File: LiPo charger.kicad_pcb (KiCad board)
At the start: 2 copper layers, 30 x 11 mm, 8 parts, among them J1 Conn_01x02, P1 USB_C_Plug_USB2.0, U1 MCP73831-2-OT

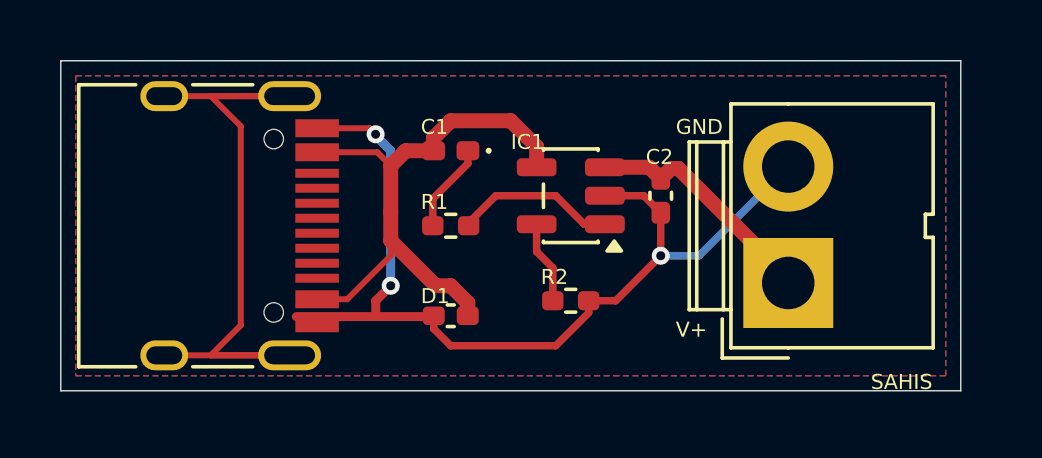
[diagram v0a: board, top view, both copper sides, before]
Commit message: PCB Trace Edited
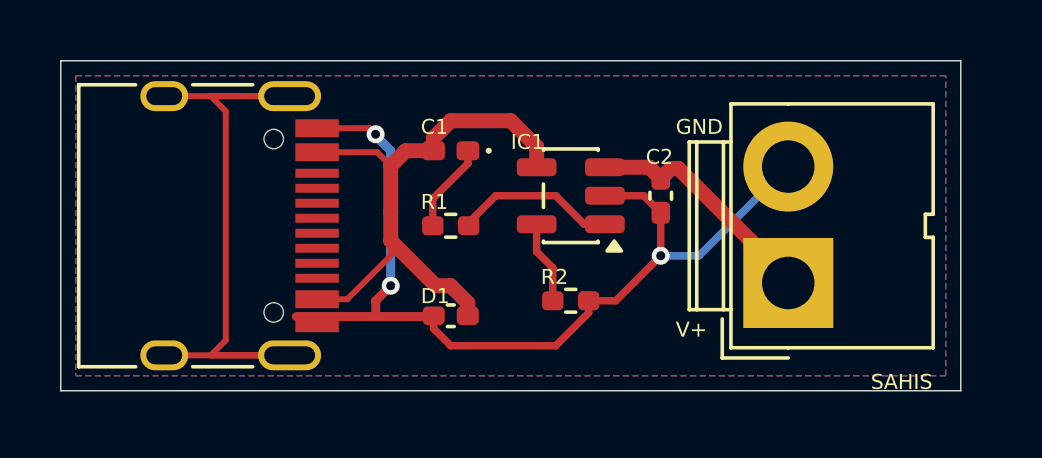
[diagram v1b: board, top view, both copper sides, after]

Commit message: changed V+ to Batt+ in front silk screen
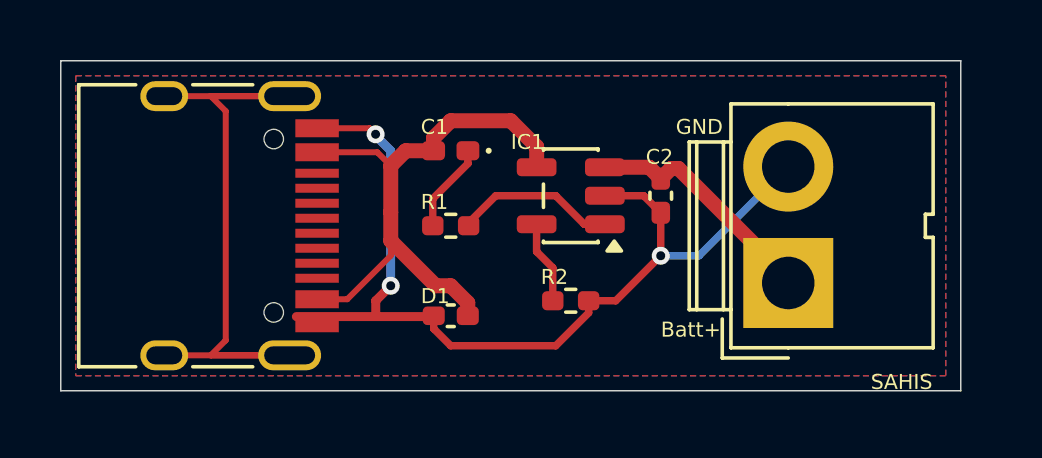
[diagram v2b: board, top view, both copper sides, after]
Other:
- board text added: "Batt+"
- board text removed: "V+"
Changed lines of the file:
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@@
 		(layer "Edge.Cuts")
 	)
-	(gr_text "GND"
-		(at 105.5 85 0)
+	(gr_text "Batt+"
+		(at 105 91.7575 0)
 		(layer "F.SilkS")
 		(effects
@@
 		)
 	)
-	(gr_text "V+"
-		(at 105.5 91.7575 0)
+	(gr_text "GND"
+		(at 105.5 85 0)
 		(layer "F.SilkS")
 		(effects
@@
 	)
 	(segment
-		(start 95.55 85.55)
-		(end 96 86)
-		(width 0.2)
-		(layer "F.Cu")
-		(net "VBUS")
-	)
-	(segment
-		(start 96 87.5475)
-		(end 96 88.5)
-		(width 0.5)
-		(layer "F.Cu")
-		(net "VBUS")
-	)
-	(segment
-		(start 96 87.5475)
-		(end 96 86)
-		(width 0.5)
-		(layer "F.Cu")
-		(net "VBUS")
-	)
-	(segment
-		(start 97.5 90)
-		(end 98 90)
-		(width 0.5)
-		(layer "F.Cu")
-		(net "VBUS")
-	)
-	(segment
-		(start 100 84.5)
-		(end 100.8625 85.3625)
-		(width 0.5)
-		(layer "F.Cu")
-		(net "VBUS")
-	)
-	(segment
-		(start 98 90)
-		(end 98.5675 90.5675)
-		(width 0.5)
-		(layer "F.Cu")
-		(net "VBUS")
-	)
-	(segment
-		(start 96 89)
-		(end 96 88.5)
-		(width 0.2)
-		(layer "F.Cu")
-		(net "VBUS")
-	)
-	(segment
-		(start 93.545 85.55)
-		(end 95.55 85.55)
-		(width 0.2)
-		(layer "F.Cu")
-		(net "VBUS")
-	)
-	(segment
-		(start 94.55 90.45)
-		(end 96 89)
-		(width 0.2)
-		(layer "F.Cu")
-		(net "VBUS")
-	)
-	(segment
-		(start 100.8625 85.3625)
-		(end 100.8625 86.05)
-		(width 0.5)
-		(layer "F.Cu")
-		(net "VBUS")
-	)
-	(segment
-		(start 98 84.5)
-		(end 100 84.5)
-		(width 0.5)
-		(layer "F.Cu")
-		(net "VBUS")
-	)
-	(segment
-		(start 96 88.5)
-		(end 97.5 90)
-		(width 0.5)
-		(layer "F.Cu")
-		(net "VBUS")
-	)
-	(segment
-		(start 97.4275 85.5)
-		(end 97.4275 85.0725)
-		(width 0.5)
-		(layer "F.Cu")
-		(net "VBUS")
-	)
-	(segment
-		(start 93.545 90.45)
-		(end 94.55 90.45)
-		(width 0.2)
-		(layer "F.Cu")
-		(net "VBUS")
-	)
-	(segment
-		(start 97.4275 85.0725)
-		(end 98 84.5)
-		(width 0.5)
-		(layer "F.Cu")
-		(net "VBUS")
-	)
-	(segment
-		(start 96.5 85.5)
-		(end 97.4275 85.5)
-		(width 0.5)
-		(layer "F.Cu")
-		(net "VBUS")
-	)
-	(segment
-		(start 96 86)
-		(end 96.5 85.5)
-		(width 0.5)
-		(layer "F.Cu")
-		(net "VBUS")
-	)
-	(segment
-		(start 98.5675 90.5675)
-		(end 98.5675 91)
-		(width 0.5)
-		(layer "F.Cu")
-		(net "VBUS")
-	)
-	(segment
 		(start 103.5 90.5)
 		(end 105 89)
@@
 	)
 	(segment
+		(start 95.55 85.55)
+		(end 96 86)
+		(width 0.2)
+		(layer "F.Cu")
+		(net "VBUS")
+	)
+	(segment
+		(start 96 87.5475)
+		(end 96 88.5)
+		(width 0.5)
+		(layer "F.Cu")
+		(net "VBUS")
+	)
+	(segment
+		(start 96 87.5475)
+		(end 96 86)
+		(width 0.5)
+		(layer "F.Cu")
+		(net "VBUS")
+	)
+	(segment
+		(start 97.5 90)
+		(end 98 90)
+		(width 0.5)
+		(layer "F.Cu")
+		(net "VBUS")
+	)
+	(segment
+		(start 100 84.5)
+		(end 100.8625 85.3625)
+		(width 0.5)
+		(layer "F.Cu")
+		(net "VBUS")
+	)
+	(segment
+		(start 98 90)
+		(end 98.5675 90.5675)
+		(width 0.5)
+		(layer "F.Cu")
+		(net "VBUS")
+	)
+	(segment
+		(start 96 89)
+		(end 96 88.5)
+		(width 0.2)
+		(layer "F.Cu")
+		(net "VBUS")
+	)
+	(segment
+		(start 93.545 85.55)
+		(end 95.55 85.55)
+		(width 0.2)
+		(layer "F.Cu")
+		(net "VBUS")
+	)
+	(segment
+		(start 94.55 90.45)
+		(end 96 89)
+		(width 0.2)
+		(layer "F.Cu")
+		(net "VBUS")
+	)
+	(segment
+		(start 100.8625 85.3625)
+		(end 100.8625 86.05)
+		(width 0.5)
+		(layer "F.Cu")
+		(net "VBUS")
+	)
+	(segment
+		(start 98 84.5)
+		(end 100 84.5)
+		(width 0.5)
+		(layer "F.Cu")
+		(net "VBUS")
+	)
+	(segment
+		(start 96 88.5)
+		(end 97.5 90)
+		(width 0.5)
+		(layer "F.Cu")
+		(net "VBUS")
+	)
+	(segment
+		(start 97.4275 85.5)
+		(end 97.4275 85.0725)
+		(width 0.5)
+		(layer "F.Cu")
+		(net "VBUS")
+	)
+	(segment
+		(start 93.545 90.45)
+		(end 94.55 90.45)
+		(width 0.2)
+		(layer "F.Cu")
+		(net "VBUS")
+	)
+	(segment
+		(start 97.4275 85.0725)
+		(end 98 84.5)
+		(width 0.5)
+		(layer "F.Cu")
+		(net "VBUS")
+	)
+	(segment
+		(start 96.5 85.5)
+		(end 97.4275 85.5)
+		(width 0.5)
+		(layer "F.Cu")
+		(net "VBUS")
+	)
+	(segment
+		(start 96 86)
+		(end 96.5 85.5)
+		(width 0.5)
+		(layer "F.Cu")
+		(net "VBUS")
+	)
+	(segment
+		(start 98.5675 90.5675)
+		(end 98.5675 91)
+		(width 0.5)
+		(layer "F.Cu")
+		(net "VBUS")
+	)
+	(segment
+		(start 90.5 91.82)
+		(end 90 92.32)
+		(width 0.2)
+		(layer "F.Cu")
+		(net "unconnected-(P1-SHIELD-PadS1)")
+	)
+	(segment
+		(start 90 83.68)
+		(end 90.5 84.18)
+		(width 0.2)
+		(layer "F.Cu")
+		(net "unconnected-(P1-SHIELD-PadS1)")
+	)
+	(segment
+		(start 88.45 92.32)
+		(end 92.63 92.32)
+		(width 0.2)
+		(layer "F.Cu")
+		(net "unconnected-(P1-SHIELD-PadS1)")
+	)
+	(segment
+		(start 90 92.32)
+		(end 92.63 92.32)
+		(width 0.2)
+		(layer "F.Cu")
+		(net "unconnected-(P1-SHIELD-PadS1)")
+	)
+	(segment
+		(start 90.5 84.18)
+		(end 90.5 91.82)
+		(width 0.2)
+		(layer "F.Cu")
+		(net "unconnected-(P1-SHIELD-PadS1)")
+	)
+	(segment
+		(start 92.63 83.68)
+		(end 90 83.68)
+		(width 0.2)
+		(layer "F.Cu")
+		(net "unconnected-(P1-SHIELD-PadS1)")
+	)
+	(segment
+		(start 88.45 83.68)
+		(end 92.63 83.68)
+		(width 0.2)
+		(layer "F.Cu")
+		(net "unconnected-(P1-SHIELD-PadS1)")
+	)
+	(segment
+		(start 92.63 83.68)
+		(end 93.031 83.68)
+		(width 0.2)
+		(layer "F.Cu")
+		(net "unconnected-(P1-SHIELD-PadS1)")
+	)
+	(segment
 		(start 103.1375 86.05)
 		(end 104.6175 86.05)
@@
 	)
 	(segment
-		(start 90.5 91.82)
-		(end 90 92.32)
-		(width 0.2)
-		(layer "F.Cu")
-		(net "unconnected-(P1-SHIELD-PadS1)")
-	)
-	(segment
-		(start 90 83.68)
-		(end 90.5 84.18)
-		(width 0.2)
-		(layer "F.Cu")
-		(net "unconnected-(P1-SHIELD-PadS1)")
-	)
-	(segment
-		(start 88.45 92.32)
-		(end 92.63 92.32)
-		(width 0.2)
-		(layer "F.Cu")
-		(net "unconnected-(P1-SHIELD-PadS1)")
-	)
-	(segment
-		(start 90 92.32)
-		(end 92.63 92.32)
-		(width 0.2)
-		(layer "F.Cu")
-		(net "unconnected-(P1-SHIELD-PadS1)")
-	)
-	(segment
-		(start 90.5 84.18)
-		(end 90.5 91.82)
-		(width 0.2)
-		(layer "F.Cu")
-		(net "unconnected-(P1-SHIELD-PadS1)")
-	)
-	(segment
-		(start 92.63 83.68)
-		(end 90 83.68)
-		(width 0.2)
-		(layer "F.Cu")
-		(net "unconnected-(P1-SHIELD-PadS1)")
-	)
-	(segment
-		(start 88.45 83.68)
-		(end 92.63 83.68)
-		(width 0.2)
-		(layer "F.Cu")
-		(net "unconnected-(P1-SHIELD-PadS1)")
-	)
-	(segment
-		(start 92.63 83.68)
-		(end 93.031 83.68)
-		(width 0.2)
-		(layer "F.Cu")
-		(net "unconnected-(P1-SHIELD-PadS1)")
-	)
-	(segment

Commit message: Changed a silk screen as SAHIS @ Branch 01
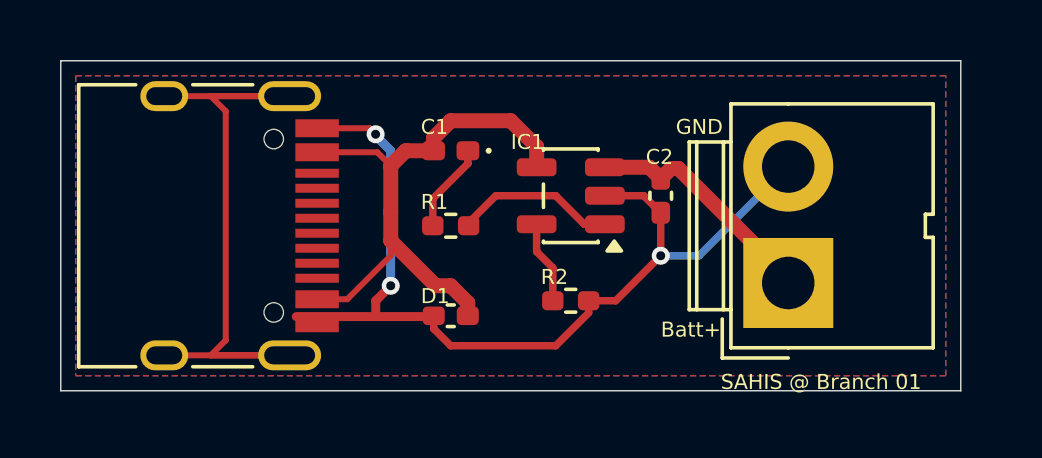
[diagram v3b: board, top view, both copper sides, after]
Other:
- board text added: "SAHIS @ Branch 01"
- board text removed: "SAHIS"
